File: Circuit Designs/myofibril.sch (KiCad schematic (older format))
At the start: 65 parts

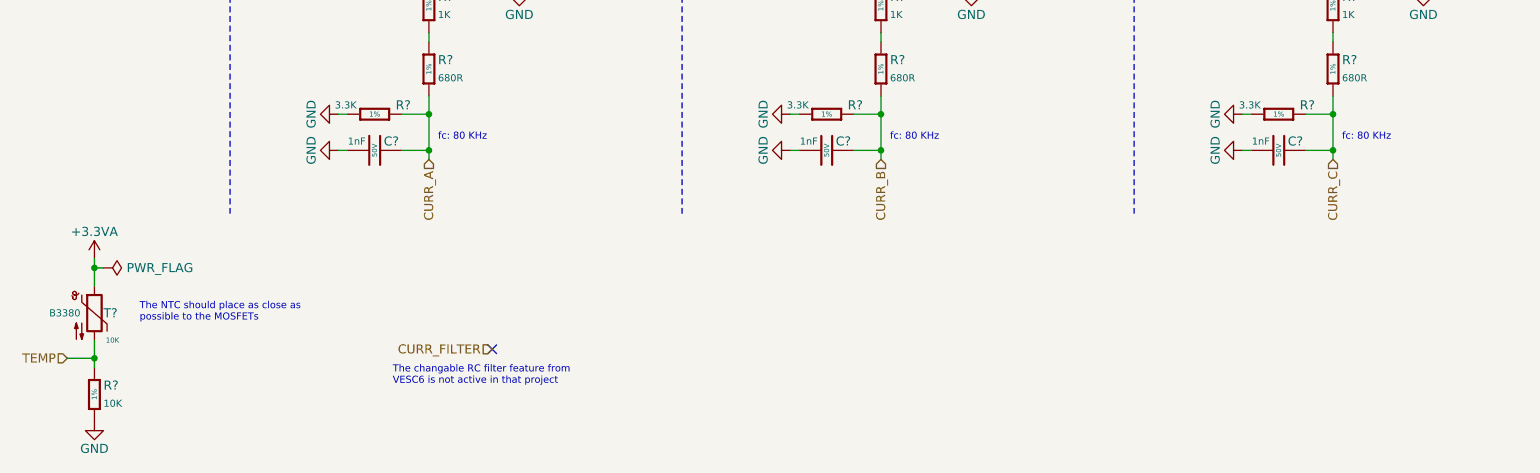
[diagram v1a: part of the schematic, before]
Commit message: edited myofibril file, added a related image about myofibrils
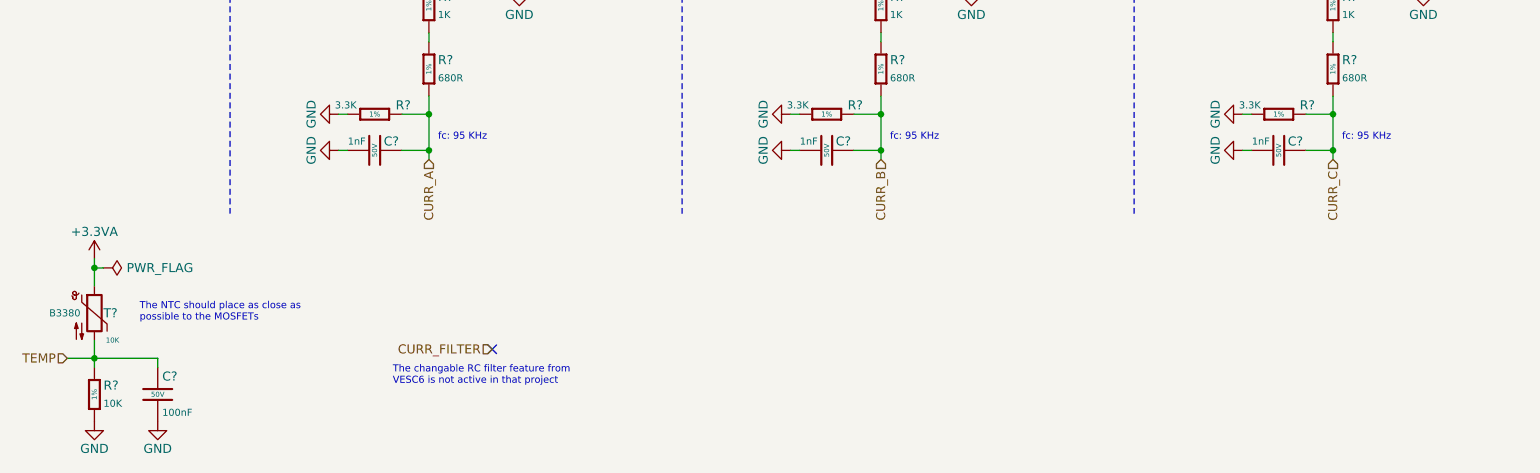
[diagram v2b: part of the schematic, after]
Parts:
- added C?: 100nF, Capacitor_SMD:C_0402_1005Metric, symbol CoE_Capacitor:100nF
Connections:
- net GND: now also C?.2
- net TEMP: now also C?.1
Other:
- note added: "fc: 95 KHz\n"
- note removed: "fc: 80 KHz\n"
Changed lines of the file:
@@
 $EndComp
 Text Notes 3150 5850 0    39   ~ 0
-fc: 80 KHz\n
+fc: 95 KHz\n
 Text HLabel 3100 5950 3    50   Input ~ 0
 CURR_A
@@
 Wire Wire Line
 	1250 7050 1250 7100
-$Comp
-L power:GND #PWR?
-U 1 1 620C3D07
-P 1250 7400
-F 0 "#PWR?" H 1250 7150 50  0001 C CNN
-F 1 "GND" H 1250 7250 50  0000 C CNN
-F 2 "" H 1250 7400 50  0001 C CNN
-F 3 "" H 1250 7400 50  0001 C CNN
-	1    1250 7400
-	1    0    0    -1
-$EndComp
 Text Notes 1500 6850 0    39   ~ 0
 The NTC should place as close as \npossible to the MOSFETs
@@
 $EndComp
 Text Notes 5650 5850 0    39   ~ 0
-fc: 80 KHz\n
+fc: 95 KHz\n
 Wire Wire Line
 	5500 4000 5500 4300
@@
 $EndComp
 Text Notes 8150 5850 0    39   ~ 0
-fc: 80 KHz\n
+fc: 95 KHz\n
 Wire Wire Line
 	8000 4000 8000 4300
@@
 Wire Wire Line
 	7600 1950 8350 1950
+$Comp
+L CoE_Capacitor:100nF C?
+U 1 1 6255591C
+P 1600 7250
+F 0 "C?" H 1625 7350 50  0000 L CNN
+F 1 "100nF" H 1625 7150 39  0000 L CNN
+F 2 "Capacitor_SMD:C_0402_1005Metric" H 1600 7650 50  0001 C BNN
+F 3 "~" H 1600 7250 50  0001 C CNN
+F 4 "50V" H 1600 7250 28  0000 C CNN "Voltage"
+F 5 "CL05B104KB54PNC" H 1600 6825 50  0001 C CNN "MFR. Part #"
+F 6 "C307331" H 1600 6725 50  0001 C CNN "JLCPCB Part #"
+	1    1600 7250
+	1    0    0    -1
+$EndComp
+Wire Wire Line
+	1600 7100 1600 7050
+Wire Wire Line
+	1600 7050 1250 7050
+$Comp
+L power:GND #PWR?
+U 1 1 620C3D07
+P 1250 7400
+F 0 "#PWR?" H 1250 7150 50  0001 C CNN
+F 1 "GND" H 1250 7250 50  0000 C CNN
+F 2 "" H 1250 7400 50  0001 C CNN
+F 3 "" H 1250 7400 50  0001 C CNN
+	1    1250 7400
+	1    0    0    -1
+$EndComp
+$Comp
+L power:GND #PWR?
+U 1 1 625729F4
+P 1600 7400
+F 0 "#PWR?" H 1600 7150 50  0001 C CNN
+F 1 "GND" H 1600 7250 50  0000 C CNN
+F 2 "" H 1600 7400 50  0001 C CNN
+F 3 "" H 1600 7400 50  0001 C CNN
+	1    1600 7400
+	1    0    0    -1
+$EndComp
 $EndSCHEMATC
